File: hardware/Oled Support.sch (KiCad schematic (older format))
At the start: 15 parts, among them J201 Conn_01x02, J202 Conn_01x02, J203 SSD1306

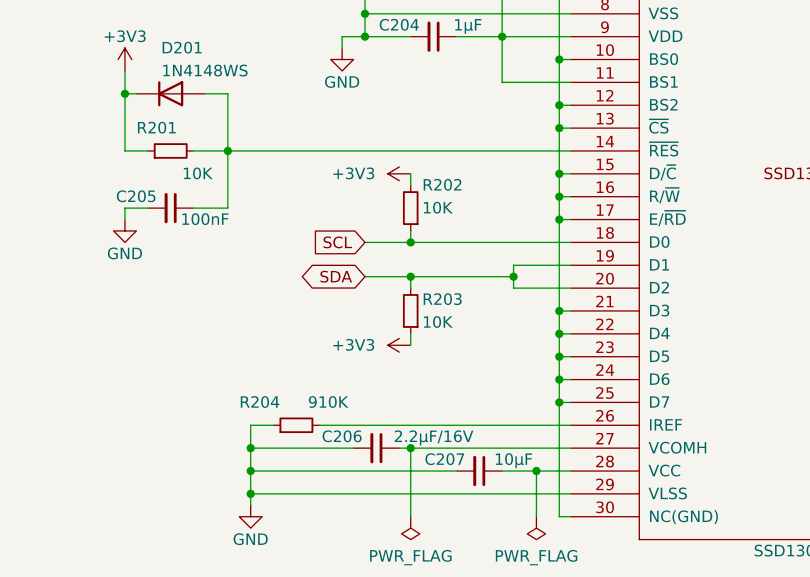
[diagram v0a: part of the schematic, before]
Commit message: Rev2 fixes
- Move I2C pullups on main board
- Fix left/right/main buttons traces
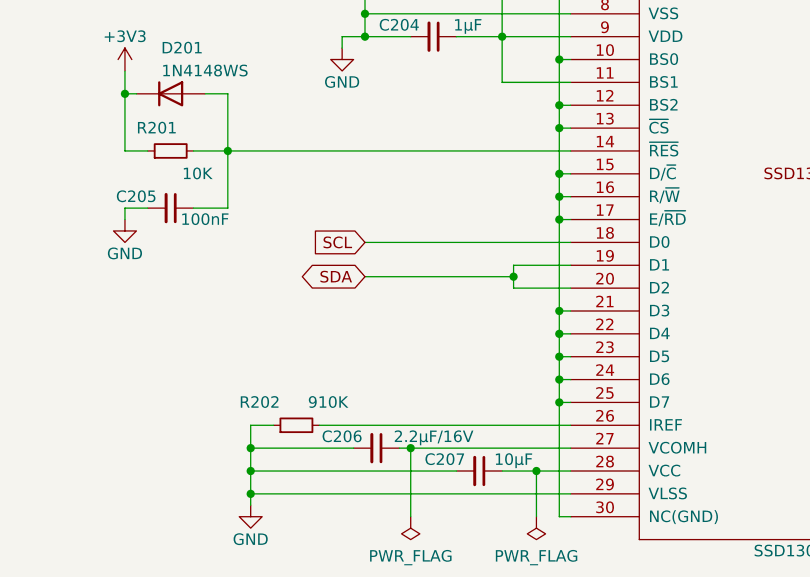
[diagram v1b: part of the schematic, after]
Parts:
- removed R202, R203: 10K, Resistor_SMD:R_0805_2012Metric_Pad1.20x1.40mm_HandSolder, symbol Device:R_Small
- D201: footprint Diode_SMD:D_SOD-323 -> Diode_SMD:D_SOD-323_HandSoldering
- renumbered R204 to R202
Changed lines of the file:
@@
 Sheet 2 2
 Title ""
-Date "2020-12-02"
-Rev "1"
+Date "2021-01-01"
+Rev "2"
 Comp ""
 Comment1 ""
@@
 AR Path="/5FC2D251" Ref="#PWR?"  Part="1"
 AR Path="/5FB24BCD/5FC2D251" Ref="#PWR?"  Part="1"
-AR Path="/5FB26E9D/5FC2D251" Ref="#PWR0208"  Part="1"
-F 0 "#PWR0208" H 2750 2950 50  0001 C CNN
+AR Path="/5FB26E9D/5FC2D251" Ref="#PWR0207"  Part="1"
+F 0 "#PWR0207" H 2750 2950 50  0001 C CNN
 F 1 "GND" H 2750 3050 50  0000 C CNN
 F 2 "" H 2750 3200 50  0001 C CNN
@@
 Wire Wire Line
 	3050 2900 3200 2900
-Wire Wire Line
-	4000 3000 4000 3050
-Wire Wire Line
-	4000 3700 4000 3750
-$Comp
-L power:+3V3 #PWR0209
-U 1 1 5FBC3AFB
-P 4000 3750
-F 0 "#PWR0209" H 4000 3600 50  0001 C CNN
-F 1 "+3V3" V 4000 4000 50  0000 C CNN
-F 2 "" H 4000 3750 50  0001 C CNN
-F 3 "" H 4000 3750 50  0001 C CNN
-	1    4000 3750
-	0    -1   -1   0
-$EndComp
-$Comp
-L power:+3V3 #PWR0207
-U 1 1 5FBC365E
-P 4000 3000
-F 0 "#PWR0207" H 4000 2850 50  0001 C CNN
-F 1 "+3V3" V 4000 3250 50  0000 C CNN
-F 2 "" H 4000 3000 50  0001 C CNN
-F 3 "" H 4000 3000 50  0001 C CNN
-	1    4000 3000
-	0    -1   -1   0
-$EndComp
-Connection ~ 4000 3300
-Wire Wire Line
-	4000 3300 3800 3300
-Connection ~ 4000 3450
-Wire Wire Line
-	4000 3450 3800 3450
-Wire Wire Line
-	4000 3450 4450 3450
-Wire Wire Line
-	4000 3450 4000 3500
-Wire Wire Line
-	4000 3300 4700 3300
-Wire Wire Line
-	4000 3300 4000 3250
-$Comp
-L Device:R_Small R?
-U 1 1 5FBB28F1
-P 4000 3600
-AR Path="/5FBB28F1" Ref="R?"  Part="1"
-AR Path="/5FB24BCD/5FBB28F1" Ref="R?"  Part="1"
-AR Path="/5FB26E9D/5FBB28F1" Ref="R203"  Part="1"
-F 0 "R203" H 3950 3550 50  0000 R CNN
-F 1 "10K" H 3950 3650 50  0000 R CNN
-F 2 "Resistor_SMD:R_0805_2012Metric_Pad1.20x1.40mm_HandSolder" H 4000 3600 50  0001 C CNN
-F 3 "" H 4000 3600 50  0001 C CNN
-F 4 "C17414" H 4000 3600 50  0001 C CNN "LCSC"
-	1    4000 3600
-	-1   0    0    1
-$EndComp
-$Comp
-L Device:R_Small R?
-U 1 1 5FBB2337
-P 4000 3150
-AR Path="/5FBB2337" Ref="R?"  Part="1"
-AR Path="/5FB24BCD/5FBB2337" Ref="R?"  Part="1"
-AR Path="/5FB26E9D/5FBB2337" Ref="R202"  Part="1"
-F 0 "R202" H 3950 3050 50  0000 R CNN
-F 1 "10K" H 3950 3150 50  0000 R CNN
-F 2 "Resistor_SMD:R_0805_2012Metric_Pad1.20x1.40mm_HandSolder" H 4000 3150 50  0001 C CNN
-F 3 "" H 4000 3150 50  0001 C CNN
-F 4 "C17414" H 4000 3150 50  0001 C CNN "LCSC"
-	1    4000 3150
-	-1   0    0    1
-$EndComp
 Text GLabel 3800 3450 0    50   BiDi ~ 0
 SDA
@@
 AR Path="/5FB2E1D7" Ref="R?"  Part="1"
 AR Path="/5FB24BCD/5FB2E1D7" Ref="R?"  Part="1"
-AR Path="/5FB26E9D/5FB2E1D7" Ref="R204"  Part="1"
-F 0 "R204" V 3600 4350 50  0000 R CNN
+AR Path="/5FB26E9D/5FB2E1D7" Ref="R202"  Part="1"
+F 0 "R202" V 3600 4350 50  0000 R CNN
 F 1 "910K" V 3600 4050 50  0000 R CNN
 F 2 "Resistor_SMD:R_0805_2012Metric_Pad1.20x1.40mm_HandSolder" H 3500 4100 50  0001 C CNN
@@
 AR Path="/5FB2E155" Ref="#PWR?"  Part="1"
 AR Path="/5FB24BCD/5FB2E155" Ref="#PWR?"  Part="1"
-AR Path="/5FB26E9D/5FB2E155" Ref="#PWR0210"  Part="1"
-F 0 "#PWR0210" H 3300 4200 50  0001 C CNN
+AR Path="/5FB26E9D/5FB2E155" Ref="#PWR0208"  Part="1"
+F 0 "#PWR0208" H 3300 4200 50  0001 C CNN
 F 1 "GND" H 3300 4300 50  0000 C CNN
 F 2 "" H 3300 4450 50  0001 C CNN
@@
 F 0 "D201" H 3000 2850 50  0000 C CNN
 F 1 "1N4148WS" H 3100 2750 50  0000 C CNN
-F 2 "Diode_SMD:D_SOD-323" H 2950 2475 50  0001 C CNN
+F 2 "Diode_SMD:D_SOD-323_HandSoldering" H 2950 2475 50  0001 C CNN
 F 3 "https://www.vishay.com/docs/85751/1n4148ws.pdf" H 2950 2650 50  0001 C CNN
 F 4 "C2128" H 2950 2650 50  0001 C CNN "LCSC"
@@
 	1    0    0    -1
 $EndComp
+Wire Wire Line
+	3800 3300 4700 3300
+Wire Wire Line
+	3800 3450 4450 3450
 $EndSCHEMATC

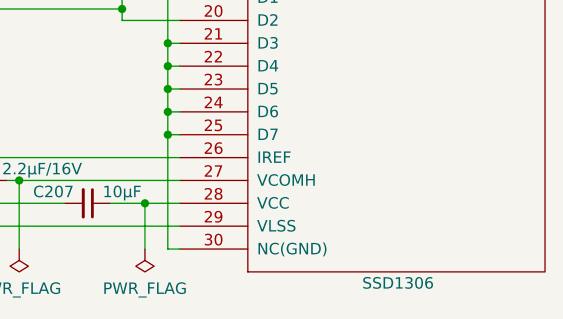
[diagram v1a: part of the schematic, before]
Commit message: SH1106 name fix
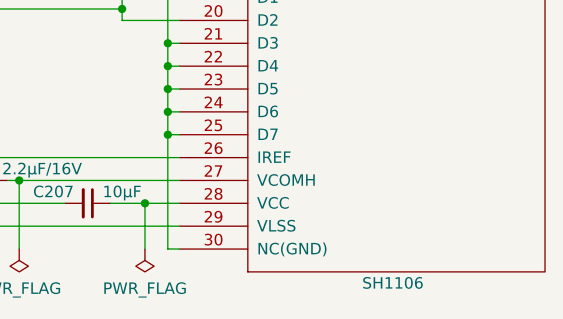
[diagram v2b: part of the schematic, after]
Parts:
- J203: value SSD1306 -> SH1106
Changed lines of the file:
@@
 AR Path="/5FB26E9D/5FB2E117" Ref="J203"  Part="1"
 F 0 "J203" H 5600 6850 50  0000 L CNN
-F 1 "SSD1306" H 5500 3650 50  0000 L CNN
+F 1 "SH1106" H 5500 3650 50  0000 L CNN
 F 2 "Display:OLED-128O064D" H 5800 5150 50  0001 C CNN
 F 3 "http://www.gabotronics.com/download/datasheets/ssd1306.pdf" H 5700 4150 50  0001 C CNN
